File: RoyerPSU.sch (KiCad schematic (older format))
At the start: 22 parts, among them J1 24VAC, J2 XLR5, J3 iso output, J4 mic out, SW1 SW_SPDT

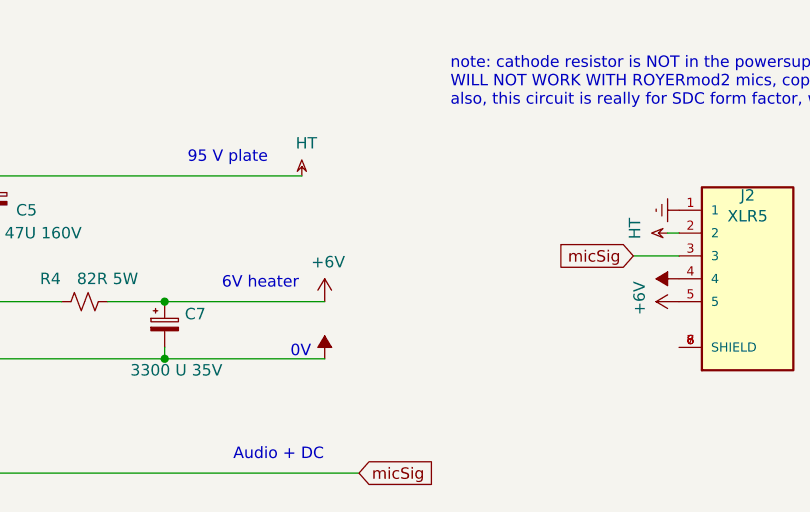
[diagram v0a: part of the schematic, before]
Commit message: added "power on" leds for voltage rails (to drain capacitors too)
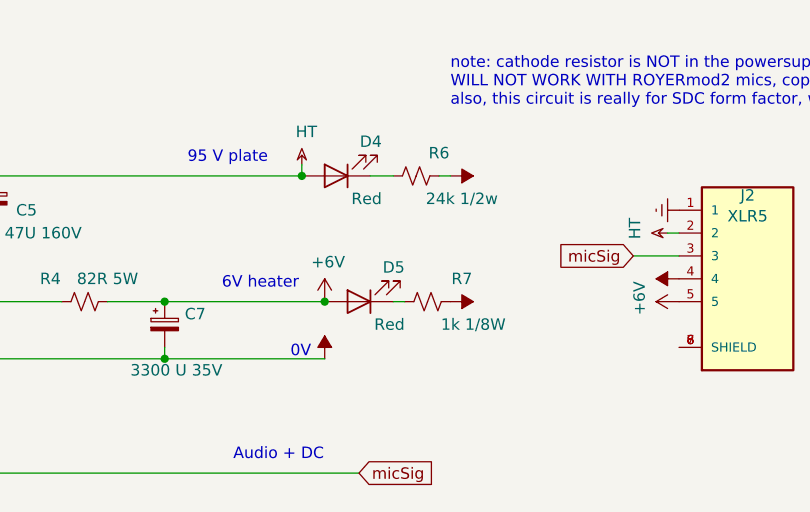
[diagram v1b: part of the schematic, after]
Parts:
- added D4, D5: Red, LED_THT:LED_D1.8mm_W1.8mm_H2.4mm_Horizontal_O1.27mm_Z1.6mm, symbol Device:LED
- added R6: 24k 1/2w, Resistor_THT:R_Axial_DIN0207_L6.3mm_D2.5mm_P7.62mm_Horizontal, symbol Device:R_Small_US
- added R7: 1k 1/8W, Resistor_THT:R_Axial_DIN0207_L6.3mm_D2.5mm_P7.62mm_Horizontal, symbol Device:R_Small_US
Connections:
- net +6V: now also D5.2 (A)
- net -BATT: now also R6.1, R7.1
- net HT: now also D4.2 (A)
- new net: D4.1 (K), R6.2
- new net: D5.1 (K), R7.2
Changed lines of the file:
@@
 	1    0    0    -1
 $EndComp
-Wire Wire Line
-	4950 1950 5200 1950
-Wire Wire Line
-	5200 1950 5900 1950
 Connection ~ 5200 1950
 Text Notes 5450 1900 0    50   ~ 0
 6V heater
-Wire Wire Line
-	4450 1400 5800 1400
 Connection ~ 4450 1400
 Text Notes 5300 1350 0    50   ~ 0
@@
 L power:HT #PWR0101
 U 1 1 60B6E63F
-P 5800 1400
-F 0 "#PWR0101" H 5800 1520 50  0001 C CNN
-F 1 "HT" H 5820 1543 50  0000 C CNN
-F 2 "" H 5800 1400 50  0001 C CNN
-F 3 "" H 5800 1400 50  0001 C CNN
-	1    5800 1400
+P 5800 1350
+F 0 "#PWR0101" H 5800 1470 50  0001 C CNN
+F 1 "HT" H 5820 1493 50  0000 C CNN
+F 2 "" H 5800 1350 50  0001 C CNN
+F 3 "" H 5800 1350 50  0001 C CNN
+	1    5800 1350
 	1    0    0    -1
 $EndComp
@@
 	1    0    0    -1
 $EndComp
+$Comp
+L Device:LED D4
+U 1 1 60EDBEB9
+P 5950 1400
+F 0 "D4" H 5750 1250 50  0000 L CNN
+F 1 "Red" H 5750 1500 50  0000 L CNN
+F 2 "LED_THT:LED_D1.8mm_W1.8mm_H2.4mm_Horizontal_O1.27mm_Z1.6mm" H 5950 1400 50  0001 C CNN
+F 3 "~" H 5950 1400 50  0001 C CNN
+	1    5950 1400
+	-1   0    0    1
+$EndComp
+$Comp
+L Device:LED D5
+U 1 1 60EDC838
+P 6050 1950
+F 0 "D5" H 5850 1800 50  0000 L CNN
+F 1 "Red" H 5850 2050 50  0000 L CNN
+F 2 "LED_THT:LED_D1.8mm_W1.8mm_H2.4mm_Horizontal_O1.27mm_Z1.6mm" H 6050 1950 50  0001 C CNN
+F 3 "~" H 6050 1950 50  0001 C CNN
+	1    6050 1950
+	-1   0    0    1
+$EndComp
+Wire Wire Line
+	5200 1950 5900 1950
+$Comp
+L power:-BATT #PWR08
+U 1 1 60EDDC47
+P 6450 1950
+F 0 "#PWR08" H 6450 1700 50  0001 C CNN
+F 1 "-BATT" H 6450 1800 50  0001 C CNN
+F 2 "" H 6450 1950 50  0001 C CNN
+F 3 "~" H 6450 1950 50  0001 C CNN
+	1    6450 1950
+	0    1    1    0
+$EndComp
+$Comp
+L power:-BATT #PWR07
+U 1 1 60EDE05E
+P 6450 1400
+F 0 "#PWR07" H 6450 1150 50  0001 C CNN
+F 1 "-BATT" H 6450 1250 50  0001 C CNN
+F 2 "" H 6450 1400 50  0001 C CNN
+F 3 "~" H 6450 1400 50  0001 C CNN
+	1    6450 1400
+	0    1    1    0
+$EndComp
+Connection ~ 5800 1400
+Wire Wire Line
+	4450 1400 5800 1400
+Connection ~ 5900 1950
+Wire Wire Line
+	4950 1950 5200 1950
+Wire Wire Line
+	5800 1350 5800 1400
+$Comp
+L Device:R_Small_US R6
+U 1 1 60EE8CEE
+P 6300 1400
+F 0 "R6" V 6200 1500 50  0000 C CNN
+F 1 "24k 1/2w" V 6400 1600 50  0000 C CNN
+F 2 "Resistor_THT:R_Axial_DIN0207_L6.3mm_D2.5mm_P7.62mm_Horizontal" H 6300 1400 50  0001 C CNN
+F 3 "~" H 6300 1400 50  0001 C CNN
+	1    6300 1400
+	0    1    1    0
+$EndComp
+$Comp
+L Device:R_Small_US R7
+U 1 1 60EE9254
+P 6350 1950
+F 0 "R7" V 6250 2100 50  0000 C CNN
+F 1 "1k 1/8W" V 6450 2150 50  0000 C CNN
+F 2 "Resistor_THT:R_Axial_DIN0207_L6.3mm_D2.5mm_P7.62mm_Horizontal" H 6350 1950 50  0001 C CNN
+F 3 "~" H 6350 1950 50  0001 C CNN
+	1    6350 1950
+	0    1    1    0
+$EndComp
+Wire Wire Line
+	6200 1400 6100 1400
+Wire Wire Line
+	6450 1400 6400 1400
+Wire Wire Line
+	6250 1950 6200 1950
 $EndSCHEMATC
